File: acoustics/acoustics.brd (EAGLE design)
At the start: 76.2 x 101.6 mm, 173 parts

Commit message: Adding power connection to acoustics
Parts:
- added U$2: 105313-1102, 105313-1102:105313-1102
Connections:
- net +3V3: now also U$2.P$1
- net GND: now also U$2.P$2
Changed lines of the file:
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@@
 <attribute name="OC_NEWARK" value="unknown" x="88.265" y="8.8392" size="1.778" layer="27" rot="R90" display="off"/>
 </element>
+<element name="U$2" library="105313-1102" package="105313-1102" value="105313-1102" x="93.1164" y="54.5592" rot="R270"/>
 </elements>
 <signals>
@@
 <vertex x="25.4508" y="0"/>
 </polygon>
+<contactref element="U$2" pad="P$1"/>
 <wire x1="69.215" y1="27.78125" x2="69.27125" y2="28.73375" width="0" layer="19" extent="1-1"/>
 </signal>
@@
 <vertex x="25.4508" y="0"/>
 </polygon>
+<contactref element="U$2" pad="P$2"/>
 <wire x1="79.53375" y1="96.04375" x2="79.59" y2="95.09125" width="0" layer="19" extent="1-1"/>
 </signal>

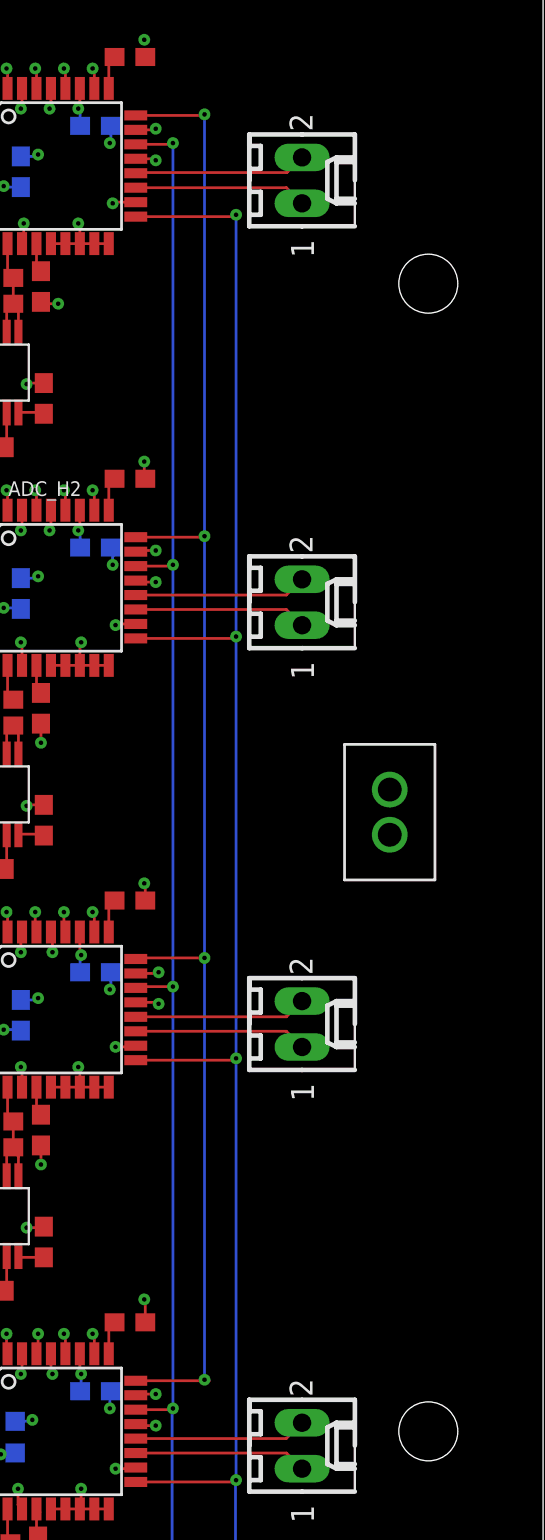
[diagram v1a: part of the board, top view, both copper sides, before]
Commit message: Fixing the power connector to add spot for nub
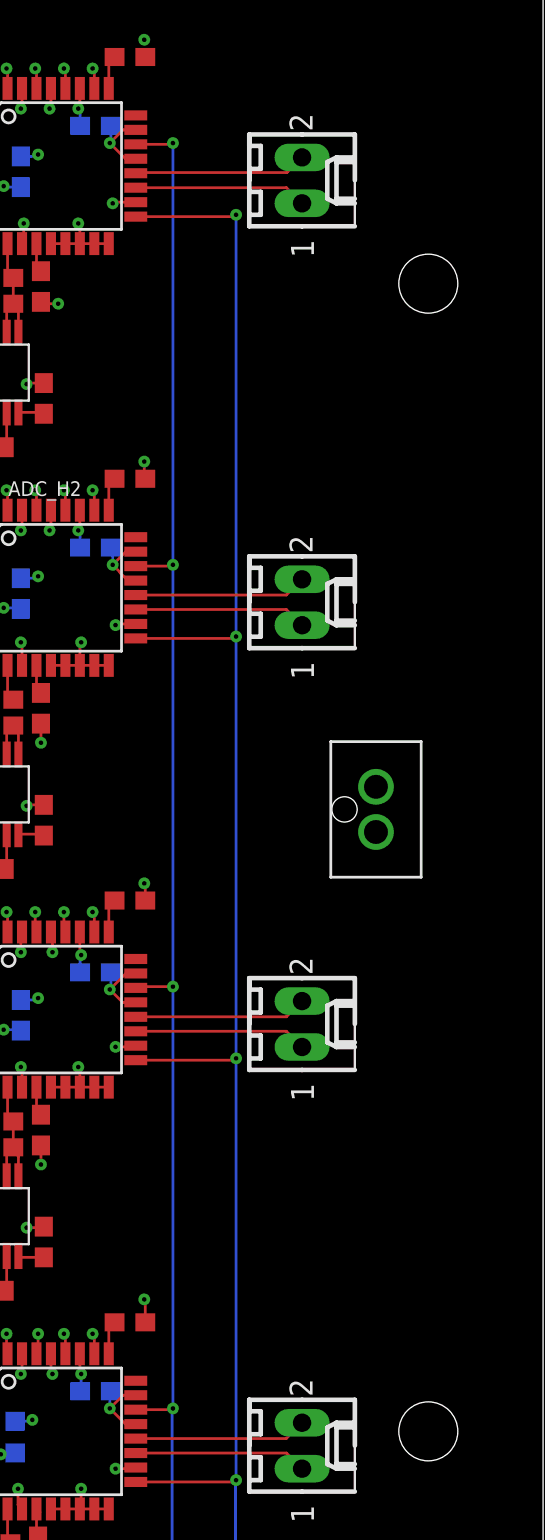
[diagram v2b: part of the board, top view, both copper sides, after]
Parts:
- moved U$2 0.78 mm to (92.4, 54.7)
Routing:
- net CLK: track 85.8 -> 0.00 mm, vias 4 -> 0
- net GND: track 138.3 -> 142.7 mm, vias 116 -> 108
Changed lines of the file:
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@@
 <setting verticaltext="up"/>
 </settings>
-<grid distance="0.006" unitdist="inch" unit="inch" style="lines" multiple="1" display="yes" altdistance="5" altunitdist="mil" altunit="mil"/>
+<grid distance="0.006" unitdist="inch" unit="inch" style="lines" multiple="1" display="no" altdistance="5" altunitdist="mil" altunit="mil"/>
 <layers>
 <layer number="1" name="Top" color="4" fill="1" visible="yes" active="yes"/>
@@
 <attribute name="OC_NEWARK" value="unknown" x="88.265" y="8.8392" size="1.778" layer="27" rot="R90" display="off"/>
 </element>
-<element name="U$2" library="105313-1102" package="105313-1102" value="105313-1102" x="93.1164" y="54.5592" rot="R270"/>
+<element name="U$2" library="105313-1102" package="105313-1102" value="105313-1102" x="92.3544" y="54.7116" rot="R270"/>
 </elements>
 <signals>
@@
 <wire x1="76.77125" y1="24.3525" x2="76.67625" y2="24.4475" width="0.1524" layer="1"/>
 <via x="76.67625" y="24.4475" extent="1-16" drill="0.25" diameter="0.55"/>
-<wire x1="79.06385" y1="21.05" x2="79.1276" y2="21.11375" width="0.1524" layer="1"/>
-<wire x1="79.1276" y1="21.11375" x2="80.16875" y2="21.11375" width="0.1524" layer="1"/>
-<via x="80.16875" y="21.11375" extent="1-16" drill="0.25" diameter="0.55"/>
 <wire x1="73.57125" y1="23.3426" x2="73.66" y2="23.43135" width="0.1524" layer="1"/>
 <wire x1="73.66" y1="23.43135" x2="73.66" y2="24.4475" width="0.1524" layer="1"/>
@@
 <contactref element="ADC_H4" pad="18"/>
 <contactref element="ADC_H4" pad="21"/>
-<wire x1="79.06385" y1="19.45" x2="79.14635" y2="19.3675" width="0.1524" layer="1"/>
-<wire x1="79.14635" y1="19.3675" x2="80.16875" y2="19.3675" width="0.1524" layer="1"/>
-<via x="80.16875" y="19.3675" extent="1-16" drill="0.25" diameter="0.55"/>
 <wire x1="79.06385" y1="17.05" x2="79.0001" y2="16.98625" width="0.1524" layer="1"/>
 <wire x1="79.0001" y1="16.98625" x2="77.94625" y2="16.98625" width="0.1524" layer="1"/>
@@
 <wire x1="77.685" y1="43.7125" x2="77.62875" y2="43.4975" width="0.1524" layer="16"/>
 <via x="77.62875" y="43.4975" extent="1-16" drill="0.25"/>
-<via x="80.3275" y="44.45" extent="1-16" drill="0.25"/>
-<via x="80.3275" y="42.70375" extent="1-16" drill="0.25"/>
-<wire x1="79.06385" y1="44.38625" x2="80.26375" y2="44.38625" width="0.1524" layer="1"/>
-<wire x1="80.26375" y1="44.38625" x2="80.3275" y2="44.45" width="0.1524" layer="1"/>
-<wire x1="79.06385" y1="42.78625" x2="80.245" y2="42.78625" width="0.1524" layer="1"/>
-<wire x1="80.245" y1="42.78625" x2="80.3275" y2="42.70375" width="0.1524" layer="1"/>
 <via x="79.53375" y="49.37125" extent="1-16" drill="0.25"/>
 <wire x1="79.53375" y1="49.37125" x2="79.59" y2="49.315" width="0.1524" layer="1"/>
@@
 <wire x1="79.59" y1="71.755" x2="79.53375" y2="71.81125" width="0.1524" layer="1"/>
 <wire x1="79.53375" y1="71.81125" x2="79.53375" y2="72.7075" width="0.1524" layer="1"/>
-<via x="80.16875" y="66.04" extent="1-16" drill="0.25"/>
-<via x="80.16875" y="67.78625" extent="1-16" drill="0.25"/>
-<wire x1="79.06385" y1="67.7225" x2="79.1276" y2="67.78625" width="0.1524" layer="1"/>
-<wire x1="79.1276" y1="67.78625" x2="80.16875" y2="67.78625" width="0.1524" layer="1"/>
-<wire x1="79.06385" y1="66.1225" x2="79.14635" y2="66.04" width="0.1524" layer="1"/>
-<wire x1="79.14635" y1="66.04" x2="80.16875" y2="66.04" width="0.1524" layer="1"/>
 <via x="77.94625" y="40.3225" extent="1-16" drill="0.25"/>
 <wire x1="79.06385" y1="40.38625" x2="79.0001" y2="40.3225" width="0.1524" layer="1"/>
@@
 <wire x1="70.47865" y1="88.65875" x2="69.45625" y2="88.65875" width="0.1524" layer="1"/>
 <wire x1="69.45625" y1="88.65875" x2="69.37375" y2="88.74125" width="0.1524" layer="1"/>
-<via x="80.16875" y="91.1225" extent="1-16" drill="0.25"/>
-<via x="80.16875" y="89.37625" extent="1-16" drill="0.25"/>
-<wire x1="79.06385" y1="91.05875" x2="80.105" y2="91.05875" width="0.1524" layer="1"/>
-<wire x1="80.105" y1="91.05875" x2="80.16875" y2="91.1225" width="0.1524" layer="1"/>
-<wire x1="79.06385" y1="89.45875" x2="80.08625" y2="89.45875" width="0.1524" layer="1"/>
-<wire x1="80.08625" y1="89.45875" x2="80.16875" y2="89.37625" width="0.1524" layer="1"/>
 <via x="54.45125" y="44.1325" extent="1-16" drill="0.25"/>
 <wire x1="54.48125" y1="45.3575" x2="54.48125" y2="44.1625" width="0.1524" layer="1"/>
@@
 <vertex x="25.4508" y="0"/>
 </polygon>
+<wire x1="79.06385" y1="91.05875" x2="78.35875" y2="91.05875" width="0.1524" layer="1"/>
+<wire x1="77.62875" y1="90.32875" x2="78.35875" y2="91.05875" width="0.1524" layer="1"/>
+<wire x1="79.06385" y1="89.45875" x2="78.49875" y2="89.45875" width="0.1524" layer="1"/>
+<wire x1="78.49875" y1="89.45875" x2="77.62875" y2="90.32875" width="0.1524" layer="1"/>
+<wire x1="79.06385" y1="21.05" x2="78.35875" y2="21.05" width="0.1524" layer="1"/>
+<wire x1="77.62875" y1="20.32" x2="78.35875" y2="21.05" width="0.1524" layer="1"/>
+<wire x1="79.06385" y1="19.45" x2="78.49875" y2="19.45" width="0.1524" layer="1"/>
+<wire x1="78.49875" y1="19.45" x2="77.62875" y2="20.32" width="0.1524" layer="1"/>
+<wire x1="79.06385" y1="42.78625" x2="78.34" y2="42.78625" width="0.1524" layer="1"/>
+<wire x1="77.62875" y1="43.4975" x2="78.34" y2="42.78625" width="0.1524" layer="1"/>
+<wire x1="79.06385" y1="44.38625" x2="78.5175" y2="44.38625" width="0.1524" layer="1"/>
+<wire x1="78.5175" y1="44.38625" x2="77.62875" y2="43.4975" width="0.1524" layer="1"/>
+<wire x1="79.06385" y1="67.7225" x2="78.5175" y2="67.7225" width="0.1524" layer="1"/>
+<wire x1="77.7875" y1="66.9925" x2="78.5175" y2="67.7225" width="0.1524" layer="1"/>
+<wire x1="78.20025" y1="66.5484125" x2="78.20025" y2="66.57975" width="0.1524" layer="1"/>
+<wire x1="78.20025" y1="66.57975" x2="77.7875" y2="66.9925" width="0.1524" layer="1"/>
+<wire x1="79.06385" y1="66.1225" x2="78.6261625" y2="66.1225" width="0.1524" layer="1"/>
+<wire x1="78.6261625" y1="66.1225" x2="78.20025" y2="66.5484125" width="0.1524" layer="1"/>
 <contactref element="U$2" pad="P$2"/>
 <wire x1="79.53375" y1="96.04375" x2="79.59" y2="95.09125" width="0" layer="19" extent="1-1"/>
@@
 <contactref element="ADC_H3" pad="24"/>
 <contactref element="ADC_H4" pad="24"/>
-<via x="82.8675" y="45.24375" extent="1-16" drill="0.25"/>
-<via x="82.8675" y="68.58" extent="1-16" drill="0.25"/>
-<via x="82.8675" y="91.91625" extent="1-16" drill="0.25"/>
-<via x="82.8675" y="21.9075" extent="1-16" drill="0.25"/>
-<wire x1="79.06385" y1="21.85" x2="83.1275" y2="21.85" width="0.1524" layer="1"/>
-<wire x1="83.1275" y1="21.85" x2="82.8675" y2="21.9075" width="0.1524" layer="1"/>
-<wire x1="82.8675" y1="21.9075" x2="82.8675" y2="45.24375" width="0.1524" layer="16"/>
-<wire x1="79.06385" y1="45.18625" x2="79.12135" y2="45.24375" width="0.1524" layer="1"/>
-<wire x1="79.12135" y1="45.24375" x2="82.8675" y2="45.24375" width="0.1524" layer="1"/>
-<wire x1="82.8675" y1="45.24375" x2="82.8675" y2="68.58" width="0.1524" layer="16"/>
-<wire x1="79.06385" y1="68.5225" x2="82.81" y2="68.5225" width="0.1524" layer="1"/>
-<wire x1="82.81" y1="68.5225" x2="82.8675" y2="68.58" width="0.1524" layer="1"/>
-<wire x1="82.8675" y1="68.58" x2="82.8675" y2="91.91625" width="0.1524" layer="16"/>
-<wire x1="79.06385" y1="91.85875" x2="82.81" y2="91.85875" width="0.1524" layer="1"/>
-<wire x1="82.81" y1="91.85875" x2="82.8675" y2="91.91625" width="0.1524" layer="1"/>
+<wire x1="79.06385" y1="68.5225" x2="79.06385" y2="91.85875" width="0" layer="19" extent="1-1"/>
+<wire x1="79.06385" y1="45.18625" x2="79.06385" y2="68.5225" width="0" layer="19" extent="1-1"/>
+<wire x1="79.06385" y1="21.85" x2="79.06385" y2="45.18625" width="0" layer="19" extent="1-1"/>
 </signal>
 </signals>

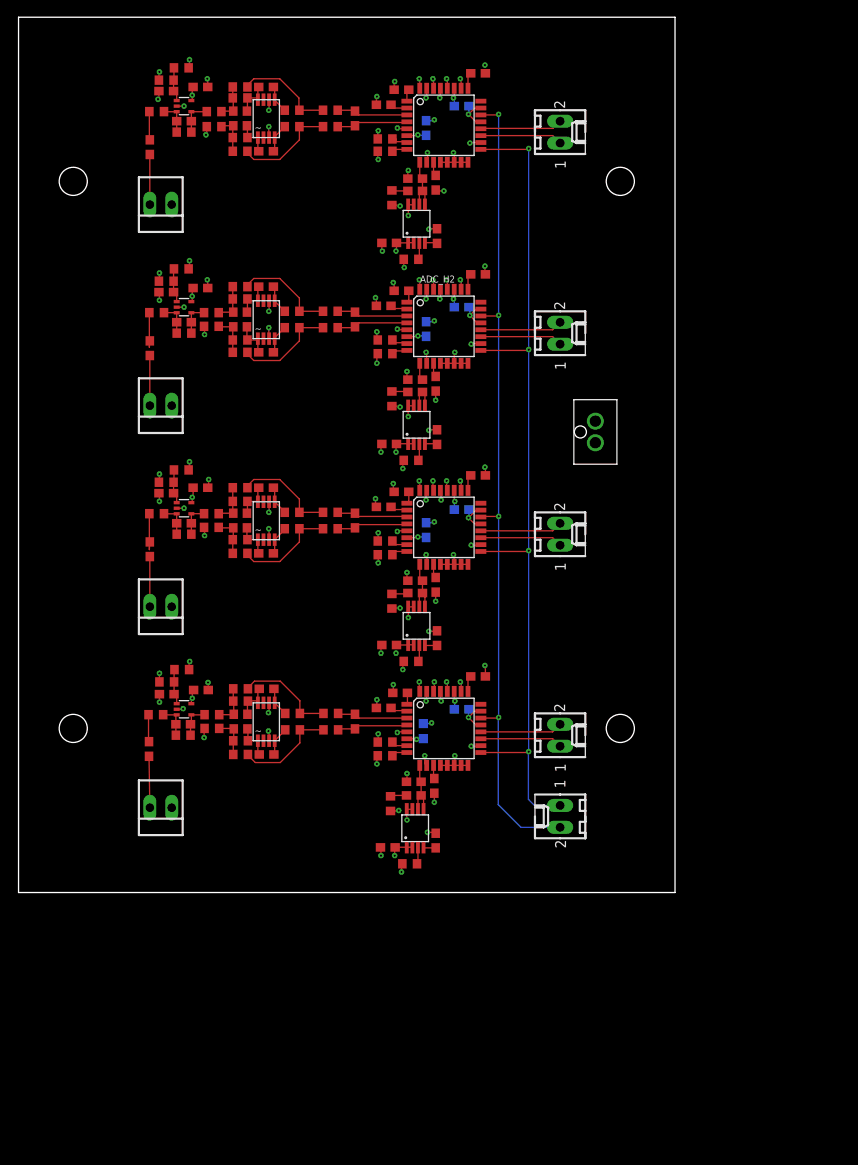
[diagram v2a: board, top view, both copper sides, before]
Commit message: Adding connectors and labels
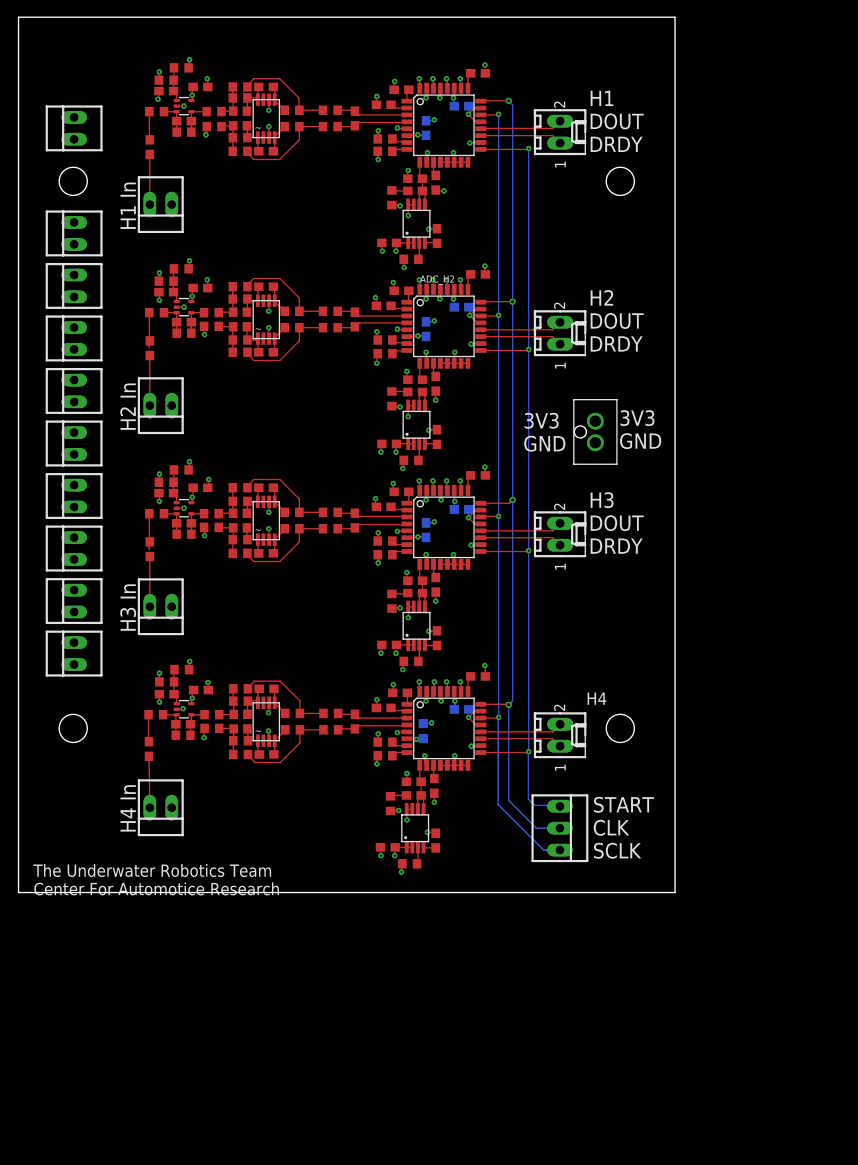
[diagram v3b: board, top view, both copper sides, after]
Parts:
- removed DCON: 22-27-2021-02, con-molex:6410-02
- added GNDPT1, GNDPT10, GNDPT2, GNDPT3, GNDPT4, GNDPT5, GNDPT6, GNDPT7, GNDPT8, GNDPT9: 22-23-2021, con-molex:22-23-2021
- added X1: 22-23-2031, con-molex:22-23-2031
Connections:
- net CLK: now also X1.2
- net GND: now also GNDPT1.1, GNDPT1.2, GNDPT10.1, GNDPT10.2, GNDPT2.1, GNDPT2.2, GNDPT3.1, GNDPT3.2, GNDPT4.1, GNDPT4.2, GNDPT5.1, GNDPT5.2, GNDPT6.1, GNDPT6.2, GNDPT7.1, GNDPT7.2, GNDPT8.1, GNDPT8.2, GNDPT9.1, GNDPT9.2
- net SCLK: now also X1.3; no longer DCON.2
- net START: now also X1.1; no longer DCON.1
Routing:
- net CLK: track 0.00 -> 102.9 mm, vias 0 -> 4
- net SCLK: track 96.9 -> 98.0 mm
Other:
- board text added: "3V3 GND"
- board text added: "H1 DOUT DRDY"
- board text added: "H1 In"
- board text added: "H2 DOUT DRDY"
- board text added: "H2 In"
- board text added: "H3 DOUT DRDY"
- board text added: "H3 In"
- board text added: "H4"
- board text added: "H4 In"
- board text added: "START CLK SCLK"
- board text added: "The Underwater Robotics Team Center For Automotice Research"

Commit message: Fixing schematic of new ADC package
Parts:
- removed ADC_H1, ADC_H2, ADC_H3, ADC_H4: ADS8322, ti-ads8322:TQFP-32
- added U1, U2, U3, U4: ADS124S08IPBSRPBS0032A_L, ADS127L01_ADC:PBS0032A_L
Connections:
- net +3V3: now also U1.27, U1.28, U1.29, U1.32, U1.6, U2.27, U2.28, U2.29, U2.32, U2.6, U3.27, U3.28, U3.29, U3.32, U3.6, U4.27, U4.28, U4.29, U4.32, U4.6; no longer ADC_H1.27, ADC_H1.28, ADC_H1.29, ADC_H1.32, ADC_H1.6, ADC_H2.27, ADC_H2.28, ADC_H2.29, ADC_H2.32, ADC_H2.6, ADC_H3.27, ADC_H3.28, ADC_H3.29, ADC_H3.32, ADC_H3.6, ADC_H4.27, ADC_H4.28, ADC_H4.29, ADC_H4.32, ADC_H4.6
- net ACD2_IN+: now also U2.4; no longer ADC_H2.4
- net ACD3_IN+: now also U3.4; no longer ADC_H3.4
- net ACD4_IN+: now also U4.4; no longer ADC_H4.4
- net ADC1_IN+: now also U1.4; no longer ADC_H1.4
- net ADC1_IN-: now also U1.3; no longer ADC_H1.3
- net ADC2_IN-: now also U2.3; no longer ADC_H2.3
- net ADC3_IN-: now also U3.3; no longer ADC_H3.3
- net ADC4_IN-: now also U4.3; no longer ADC_H4.3
- net CLK: now also U1.24, U2.24, U3.24, U4.24; no longer ADC_H1.24, ADC_H2.24, ADC_H3.24, ADC_H4.24
- net DOUT_H1: now also U1.20; no longer ADC_H1.20
- net DOUT_H2: now also U2.20; no longer ADC_H2.20
- net DOUT_H3: now also U3.20; no longer ADC_H3.20
- net DOUT_H4: now also U4.20; no longer ADC_H4.20
- net DRDY_H1: now also U1.19; no longer ADC_H1.19
- net DRDY_H2: now also U2.19; no longer ADC_H2.19
- net DRDY_H3: now also U3.19; no longer ADC_H3.19
- net DRDY_H4: now also U4.19; no longer ADC_H4.19
- net GND: now also U1.10, U1.12, U1.13, U1.14, U1.15, U1.16, U1.18, U1.21, U1.23, U1.26, U1.30, U1.31, U1.5, U2.10, U2.12, U2.13, U2.14, U2.15, U2.16, U2.18, U2.21, U2.23, U2.26, U2.30, U2.31, U2.5, U3.10, U3.12, U3.13, U3.14, U3.15, U3.16, U3.18, U3.21, U3.23, U3.26, U3.30, U3.31, U3.5, U4.10, U4.12, U4.13, U4.14, U4.15, U4.16, U4.18, U4.21, U4.23, U4.26, U4.30, U4.31, U4.5; no longer ADC_H1.10, ADC_H1.12, ADC_H1.13, ADC_H1.14, ADC_H1.15, ADC_H1.16, ADC_H1.18, ADC_H1.21, ADC_H1.23, ADC_H1.26, ADC_H1.30, ADC_H1.31, ADC_H1.5, ADC_H2.10, ADC_H2.12, ADC_H2.13, ADC_H2.14, ADC_H2.15, ADC_H2.16, ADC_H2.18, ADC_H2.21, ADC_H2.23, ADC_H2.26, ADC_H2.30, ADC_H2.31, ADC_H2.5, ADC_H3.10, ADC_H3.12, ADC_H3.13, ADC_H3.14, ADC_H3.15, ADC_H3.16, ADC_H3.18, ADC_H3.21, ADC_H3.23, ADC_H3.26, ADC_H3.30, ADC_H3.31, ADC_H3.5, ADC_H4.10, ADC_H4.12, ADC_H4.13, ADC_H4.14, ADC_H4.15, ADC_H4.16, ADC_H4.18, ADC_H4.21, ADC_H4.23, ADC_H4.26, ADC_H4.30, ADC_H4.31, ADC_H4.5
- net H4_REFV: now also U4.9; no longer ADC_H4.9
- net N$1: now also U2.1; no longer ADC_H2.1
- net N$11: now also U4.1; no longer ADC_H4.1
- net N$12: now also U3.1; no longer ADC_H3.1
- net N$13: now also U2.25; no longer ADC_H2.25
- net N$18: now also U3.7; no longer ADC_H3.7
- net N$21: now also U3.11; no longer ADC_H3.11
- net N$22: now also U2.8; no longer ADC_H2.8
- net N$23: now also U3.8; no longer ADC_H3.8
- net N$24: now also U4.2; no longer ADC_H4.2
- net N$3: now also U2.2; no longer ADC_H2.2
- net N$30: now also U3.25; no longer ADC_H3.25
- net N$31: now also U4.8; no longer ADC_H4.8
- net N$32: now also U4.7; no longer ADC_H4.7
- net N$35: now also U4.11; no longer ADC_H4.11
- net N$37: now also U3.9; no longer ADC_H3.9
- net N$38: now also U4.25; no longer ADC_H4.25
- net N$39: now also U1.1; no longer ADC_H1.1
- net N$4: now also U2.7; no longer ADC_H2.7
- net N$40: now also U1.2; no longer ADC_H1.2
- net N$44: now also U1.7; no longer ADC_H1.7
- net N$45: now also U1.8; no longer ADC_H1.8
- net N$48: now also U1.11; no longer ADC_H1.11
- net N$56: now also U1.25; no longer ADC_H1.25
- net N$6: now also U1.9; no longer ADC_H1.9
- net N$8: now also U3.2; no longer ADC_H3.2
- net N$9: now also U2.11; no longer ADC_H2.11
- net POSITIVE_REF: now also U2.9; no longer ADC_H2.9
- net SCLK: now also U1.22, U2.22, U3.22, U4.22; no longer ADC_H1.22, ADC_H2.22, ADC_H3.22, ADC_H4.22
- net START: now also U1.17, U2.17, U3.17, U4.17; no longer ADC_H1.17, ADC_H2.17, ADC_H3.17, ADC_H4.17
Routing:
- net GND: track 142.7 -> 92.3 mm, vias 108 -> 80
- net +3V3: track 58.3 -> 35.4 mm, vias 36 -> 24
- net START: track 101.9 -> 80.1 mm
- net DRDY_H4: track 9.66 -> 1.22 mm
- net DRDY_H1: track 9.56 -> 1.22 mm
- net DOUT_H3: track 9.56 -> 1.23 mm
- net DOUT_H2: track 9.56 -> 1.23 mm
- net DRDY_H3: track 9.56 -> 1.23 mm
- net DRDY_H2: track 9.56 -> 1.23 mm
- net DOUT_H4: track 9.56 -> 1.24 mm
- net CLK: track 102.9 -> 96.3 mm
- net SCLK: track 98.0 -> 91.7 mm
- net ADC4_IN-: track 8.21 -> 2.62 mm
- net ADC2_IN-: track 8.26 -> 2.68 mm
- net ADC1_IN-: track 8.26 -> 2.68 mm
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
